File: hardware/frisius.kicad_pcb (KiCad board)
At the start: 4 copper layers, 40 x 60 mm, 133 parts, among them J1 Conn_02x20_Odd_Even_Shielded, J3 USB_C_Receptacle, J4 MEM2067, Q1 Q_NMOS_DGS, Q2 MBT2222ADW1T1, SW1 OVERRIDE, SW2 SW_Push, SW3 SW_Push, SW4 SW_Push, U1 ESP32-PICO-V3-02, U10 CP2102N-Axx-xQFN24, U12 RT5789, U13 MAX8881EUT33+T, U2 FXOS8700CQR1, U3 MS5637-02BA03, U4 L96-M33, U5 MAX77751, U6 LM75B, U7 MAX17048G

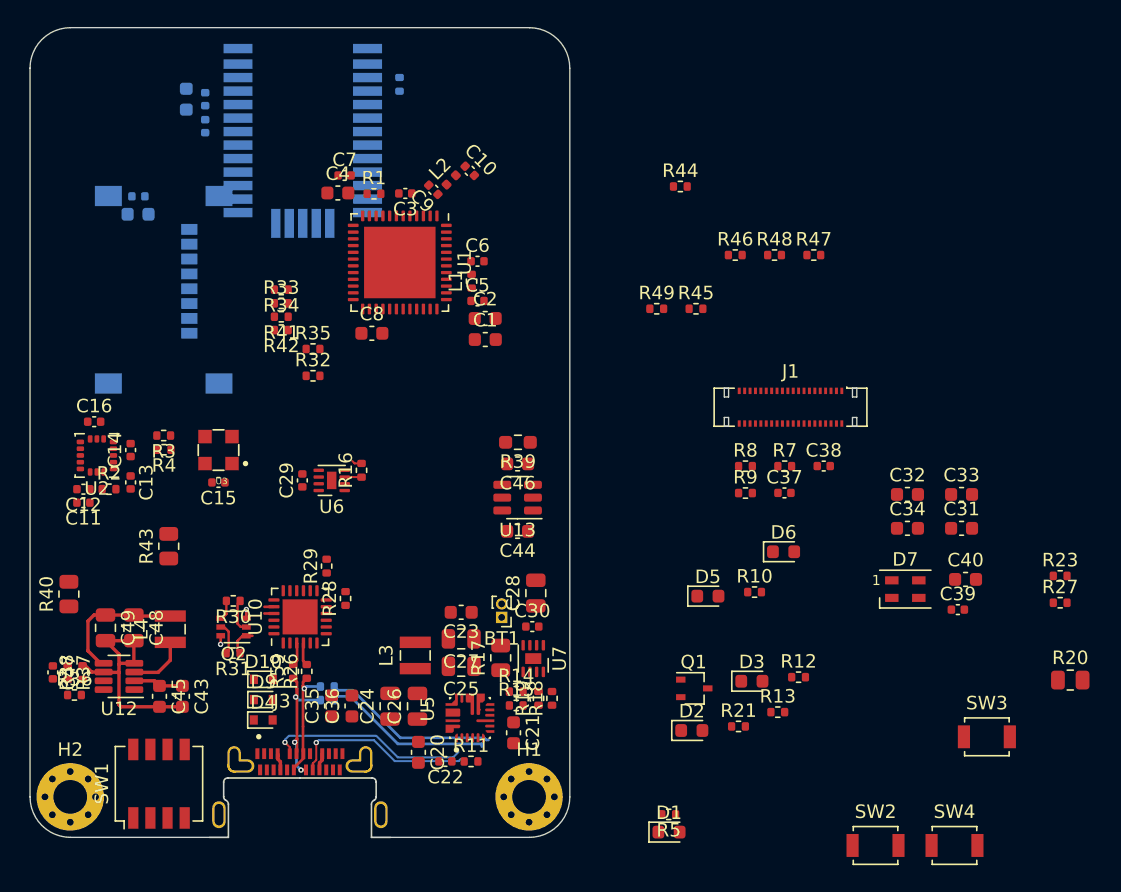
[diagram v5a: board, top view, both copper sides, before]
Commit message: schematic tidy up, component placement, shielding investigation
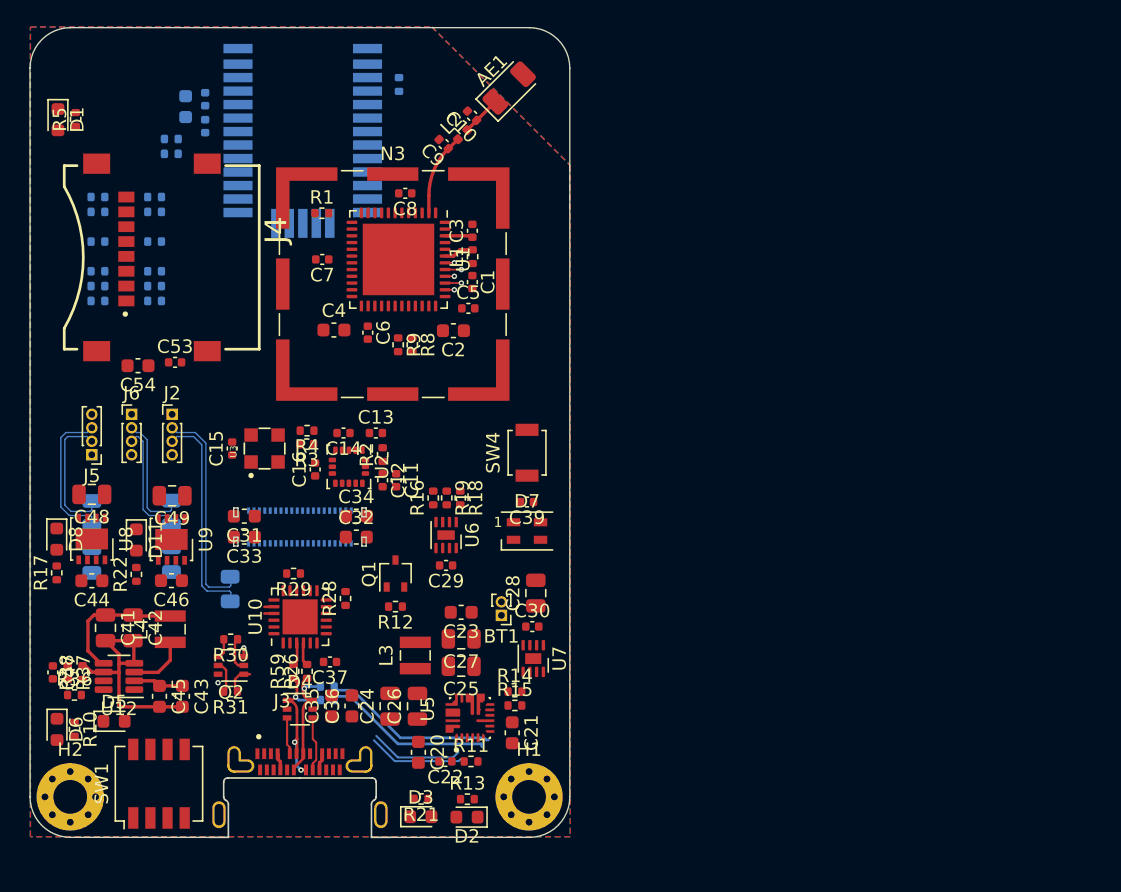
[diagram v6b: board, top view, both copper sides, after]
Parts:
- removed C38: 0.1u, Capacitor_SMD:C_0402_1005Metric
- removed C40: 1u, Capacitor_SMD:C_0603_1608Metric
- removed D10, D9: TVS, Diode_SMD:D_SOD-523
- removed R7: 0, Resistor_SMD:R_0402_1005Metric
- removed SW2, SW3: SW_Push, Button_Switch_SMD:SW_SPST_B3U-1000P
- removed U13: MAX8881EUT33+T, Package_TO_SOT_SMD:SOT-23-6
- added AE1: 2.4G, RF_Antenna:Johanson_2450AT18x100, F.Cu at (150.1, 38.4)
- added C41: 10u, Capacitor_SMD:C_0805_2012Metric, F.Cu at (120.2, 78.4)
- added C42: 10u, Capacitor_SMD:C_0805_2012Metric, F.Cu at (122.2, 78.4)
- added D11: LED_Small_Filled, LED_SMD:LED_0603_1608Metric, F.Cu at (122.5, 71.9)
- added D8: LED_Small_Filled, LED_SMD:LED_0603_1608Metric, F.Cu at (116.6, 71.8)
- added J2: Conn_01x04_Male, Connector_PinHeader_1.00mm:PinHeader_1x04_P1.00mm_Vertical, F.Cu at (125.2, 62.5)
- added J5: Conn_01x04_Male, Connector_PinHeader_1.00mm:PinHeader_1x04_P1.00mm_Vertical, F.Cu at (119.2, 65.5)
- added J6: Conn_01x04_Male, Connector_PinHeader_1.00mm:PinHeader_1x04_P1.00mm_Vertical, F.Cu at (122.2, 62.5)
- added N3: ShieldCan_ESP, RF_Shielding:Laird_Technologies_BMI-S-102_16.50x16.50mm, F.Cu at (141.5, 52.9)
- added R22: 1k, Resistor_SMD:R_0402_1005Metric, F.Cu at (122.5, 74.4)
- added R50: 0, Resistor_SMD:R_0805_2012Metric, B.Cu at (125.1, 73.3)
- added U8: NCV8187AMLExCG, Package_DFN_QFN:DFN-8-1EP_3x3mm_P0.65mm_EP1.55x2.4mm, F.Cu at (119.2, 71.8)
- added U9: NCV8187AMLExCG, Package_DFN_QFN:DFN-8-1EP_3x3mm_P0.65mm_EP1.55x2.4mm, F.Cu at (125.1, 71.8)
- C1, C8: value 1u -> 0.1u; footprint Capacitor_SMD:C_0603_1608Metric -> Capacitor_SMD:C_0402_1005Metric
- C46: value 4.7u -> 1u
- C53, C54, J4: moved to F.Cu
- D4: value TVS -> ESD5V5U5ULCE6327HTSA1; footprint Diode_SMD:D_SOD-523 -> Package_TO_SOT_SMD:SOT-363_SC-70-6
- J1, R20, R23, R27, R32, R33, R34, R35, R40, R41, R42, R43, R44, R45, R46, R47, R48, R49: moved to B.Cu
- R17: value 0 -> 1k; footprint Resistor_SMD:R_0805_2012Metric -> Resistor_SMD:R_0402_1005Metric
- R39: footprint Resistor_SMD:R_0603_1608Metric_Pad0.98x0.95mm_HandSolder -> Resistor_SMD:R_0805_2012Metric; moved to B.Cu
- moved R27 74.3 mm to (125.1, 42.1)
- moved R23 72.9 mm to (125.1, 43.2)
- moved D1 69.5 mm to (116.7, 40.7), turned to -90 degrees
- moved R5 67.7 mm to (118.0, 40.7), turned to 90 degrees
- moved R20 62.6 mm to (129.4, 75.5), turned to 90 degrees
- moved D6 55.4 mm to (116.6, 85.9), turned to -90 degrees
- moved C33 53.2 mm to (130.5, 71.7), turned to 180 degrees
- moved C31 53.2 mm to (130.5, 70.1), turned to 180 degrees
- moved R47 53.1 mm to (119.7, 49.8)
- moved R10 51.4 mm to (117.9, 85.9), turned to -90 degrees
- moved R48 50.2 mm to (119.7, 47.5)
- moved R46 47.2 mm to (119.7, 52.0)
- moved D5 45.0 mm to (120.8, 85.3)
- moved R45 44.4 mm to (119.7, 53.0)
- moved R44 44.0 mm to (119.7, 54.1)
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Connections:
- C17 pad 1: VCC_BKUP_3V3 -> VDD_NVDC
- C29 pad 1: +BATT -> VDD_NVDC
- C31 pad 2: Net-(J1-Pad1) -> Net-(C31-Pad2)
- C32 pad 1: VCC_BKUP_3V3 -> VDD_NVDC
- C32 pad 2: Net-(J1-Pad1) -> Net-(C31-Pad2)
- C33 pad 2: Net-(J1-Pad1) -> Net-(C31-Pad2)
- C34 pad 1: VCC_BKUP_3V3 -> VDD_NVDC
- C34 pad 2: Net-(J1-Pad1) -> Net-(C31-Pad2)
- C37 pad 2: VDD_USB_3V3 -> 3V3_CORE
- C44 pad 1: VDD_NVDC -> VDD_SYS_3V5
- C46 pad 1: Net-(C46-Pad1) -> VDD_SYS_3V5
- C47 pad 1: Net-(C47-Pad1) -> VDD_SYS_3V5
- C48 pad 1: Net-(C47-Pad1) -> /Power/VDD_AUX_S+
- C49 pad 1: Net-(C47-Pad1) -> /Power/VDD_CORE_S+
- C6 pad 1: /Processor/3V3_ESP_VDDA_FILT -> Net-(C6-Pad1)
- C8 pad 1: Net-(C8-Pad1) -> /Processor/3V3_ESP_VDDA_FILT
- D4 pad 1: GND -> /USB/PORT_D+
- D4 pad 2: VBUS -> GND
- D5 pad 2: /Display B2B/USR_BTN.PWR -> /Power/BOOTSTRAP
- D6 pad 2: Net-(C47-Pad1) -> Net-(D6-Pad2)
- J1 pad 1: Net-(J1-Pad1) -> Net-(C31-Pad2)
- J1 pad 11: Net-(J1-Pad1) -> Net-(C31-Pad2)
- J1 pad 12: Net-(J1-Pad1) -> Net-(C31-Pad2)
- J1 pad 13: Net-(J1-Pad1) -> unconnected-(J1-Pad13)
- J1 pad 14: Net-(J1-Pad1) -> unconnected-(J1-Pad14)
- J1 pad 17: Net-(J1-Pad1) -> Net-(C31-Pad2)
- J1 pad 2: Net-(J1-Pad1) -> Net-(C31-Pad2)
- J1 pad 22: Net-(J1-Pad1) -> Net-(C31-Pad2)
- J1 pad 28: Net-(J1-Pad1) -> Net-(C31-Pad2)
- J1 pad 29: Net-(J1-Pad1) -> Net-(C31-Pad2)
- J1 pad 3: Net-(J1-Pad1) -> Net-(C31-Pad2)
- J1 pad 33: Net-(J1-Pad1) -> Net-(C31-Pad2)
- J1 pad 34: Net-(J1-Pad1) -> Net-(C31-Pad2)
- J1 pad 35: VCC_BKUP_3V3 -> VDD_NVDC
- J1 pad 36: VCC_BKUP_3V3 -> VDD_NVDC
- J1 pad 37: VCC_BKUP_3V3 -> VDD_NVDC
- J1 pad 38: VCC_BKUP_3V3 -> VDD_NVDC
- J1 pad 39: Net-(J1-Pad1) -> Net-(C31-Pad2)
- J1 pad 4: Net-(J1-Pad1) -> Net-(C31-Pad2)
- J1 pad 40: Net-(J1-Pad1) -> Net-(C31-Pad2)
- L4 pad 2: Net-(C47-Pad1) -> VDD_SYS_3V5
- R10 pad 1: GND -> VDD_NVDC
- R10 pad 2: Net-(D6-Pad1) -> Net-(D6-Pad2)
- R17 pad 1: Net-(R17-Pad1) -> VDD_SYS_3V5
- R17 pad 2: +BATT -> Net-(D8-Pad2)
- R18 pad 1: 3V3_CORE -> VDD_AUX_3V3
- R19 pad 1: 3V3_CORE -> VDD_AUX_3V3
- R20 pad 1: Net-(R20-Pad1) -> VDD_SYS_3V5
- R20 pad 2: VDD_DISP_3V3 -> VDD_DISP_3V5
- R28 pad 2: VDD_USB_3V3 -> 3V3_CORE
- R36 pad 2: Net-(C47-Pad1) -> VDD_SYS_3V5
- R37 pad 1: Net-(C47-Pad1) -> VDD_SYS_3V5
- R39 pad 1: Net-(C46-Pad1) -> VDD_SYS_3V5
- R39 pad 2: VCC_BKUP_3V3 -> /Power/VDD_AUX_S+
- R40 pad 1: Net-(C47-Pad1) -> /Power/VDD_CORE_S+
- R43 pad 1: VDD_SYS_3V3 -> /Power/VDD_AUX_S+
- U1 pad 10: /Display B2B/USR_BTN.PWR -> /Processor/USR_BTN.PWR
- U1 pad 26: Net-(C8-Pad1) -> Net-(C6-Pad1)
- U1 pad 8: /Display B2B/USR_BTN.NAV_A -> /Processor/USR_BTN.NAV_A
- U10 pad 5: VDD_USB_3V3 -> 3V3_CORE
- U10 pad 6: VDD_USB_3V3 -> 3V3_CORE
- U10 pad 7: Net-(R7-Pad1) -> 3V3_CORE
- U12 pad 1: unconnected-(U12-Pad1) -> Net-(D6-Pad1)
- U12 pad 5: Net-(C47-Pad1) -> VDD_SYS_3V5
- U4 pad 8: VCC_BKUP_3V3 -> VDD_NVDC
- U6 pad 8: +BATT -> VDD_NVDC
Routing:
- net VDD_SYS_3V5: track 0.00 -> 26.1 mm
- net VDD_DISP_3V5: track 0.00 -> 16.1 mm
- net /Power/VDD_AUX_S+: track 0.00 -> 11.0 mm
- net Net-(C47-Pad1): track 10.1 -> 0.00 mm
- net VDD_AUX_3V3: track 0.00 -> 10.0 mm
- net 3V3_CORE: track 0.00 -> 9.19 mm
- net /Power/VDD_CORE_S+: track 0.00 -> 9.17 mm
- net Net-(C9-Pad1): track 0.00 -> 6.12 mm
- net /Processor/3V3_ESP_VDDA_FILT: track 0.00 -> 4.26 mm
- net /BMS/USB_CC.1: track 15.0 -> 11.5 mm, vias 1 -> 0
- net Net-(AE1-Pad1): track 0.00 -> 2.95 mm
- net /BMS/USB_CC.2: track 13.6 -> 11.2 mm, vias 1 -> 0
- net /BMS/THERM_SHDN: track 1.25 -> 0.00 mm
- net /Processor/DEBUG_UART.TXD: track 0.00 -> 1.21 mm, vias 0 -> 1
- net /Display B2B/DISPLAY.DC: track 0.00 -> 1.21 mm, vias 0 -> 1
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- added copper zone on B.Cu, net GND
- added copper zone on F.Cu, net GND

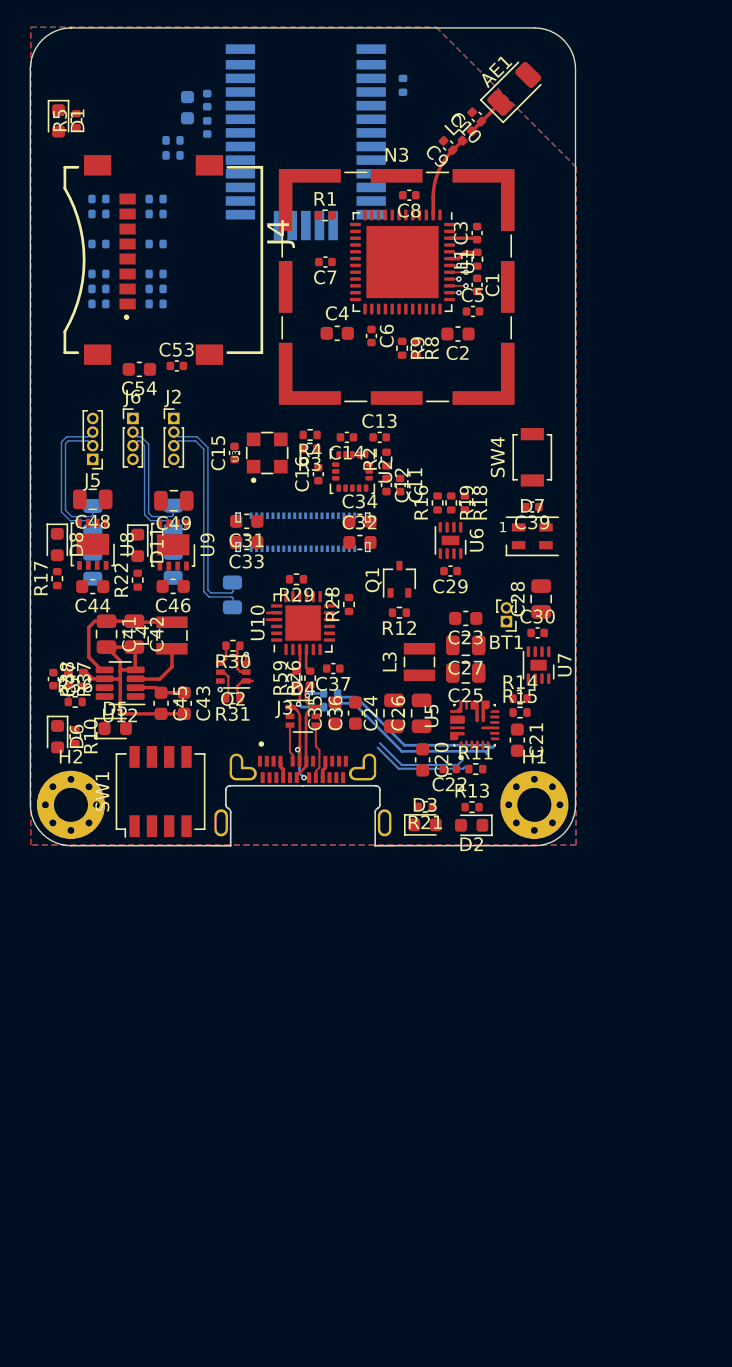
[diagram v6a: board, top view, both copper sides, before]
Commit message: minor sch tweaks, more layout, added power emc shield
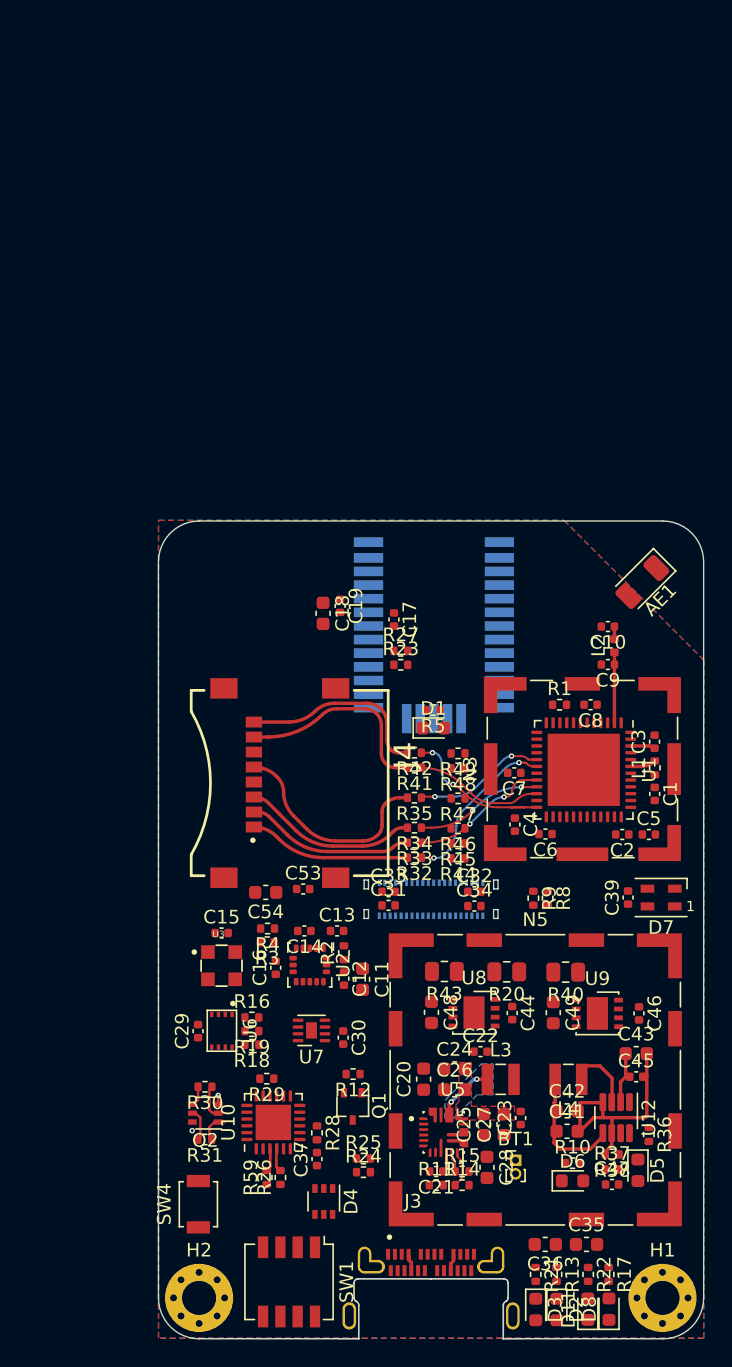
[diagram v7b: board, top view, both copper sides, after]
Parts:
- removed J2, J5, J6: Conn_01x04_Male, Connector_PinHeader_1.00mm:PinHeader_1x04_P1.00mm_Vertical
- removed R39, R50: 0, Resistor_SMD:R_0805_2012Metric
- removed R6: 0, Resistor_SMD:R_0402_1005Metric
- added N5: SheildCan_Power, RF_Shielding:Wuerth_36103205_20x20mm, F.Cu at (151.7, 111.1)
- C11: footprint Capacitor_SMD:C_0402_1005Metric -> Capacitor_SMD:C_0603_1608Metric
- C17, C18, C19, R20, R23, R24, R25, R27, R32, R33, R34, R35, R40, R41, R42, R43, R44, R45, R46, R47, R48, R49: moved to F.Cu
- C2, C31, C32, C33, C34, C4, C44, C45, C46: footprint Capacitor_SMD:C_0603_1608Metric -> Capacitor_SMD:C_0402_1005Metric
- C21, C23: value 4.7u -> 1u; footprint Capacitor_SMD:C_0603_1608Metric -> Capacitor_SMD:C_0402_1005Metric
- C24, C25, C26, C27, C28, C41, C42, C48, C49: footprint Capacitor_SMD:C_0805_2012Metric -> Capacitor_SMD:C_0603_1608Metric
- N3: footprint RF_Shielding:Laird_Technologies_BMI-S-102_16.50x16.50mm -> RF_Shielding:Laird_Technologies_BMI-S-101_13.66x12.70mm
- U6: footprint Package_DFN_QFN:DFN-8-1EP_2x2mm_P0.5mm_EP0.7x1.3mm -> bt_Package_SON:XSON-8U
- moved D8 69.2 mm to (157.1, 127.9), turned to 90 degrees
- moved R17 65.1 mm to (157.1, 125.3), turned to -90 degrees
- moved D11 65.0 mm to (155.5, 127.9), turned to 90 degrees
- moved R22 60.7 mm to (155.6, 125.3), turned to -90 degrees
- moved SW4 60.0 mm to (127.0, 120.2)
- moved C47 55.3 mm to (157.3, 118.8), turned to 0 degrees
- moved R37 53.7 mm to (157.3, 117.7), turned to 0 degrees
- moved R36 52.7 mm to (160.0, 115.1), turned to -90 degrees
- moved D1 52.3 mm to (144.2, 85.3), turned to 0 degrees
- moved R38 52.2 mm to (157.3, 116.5), turned to 180 degrees
- moved R5 50.6 mm to (144.2, 84.0), turned to 180 degrees
- moved D5 50.2 mm to (159.2, 117.7), turned to -90 degrees
- moved D6 49.9 mm to (154.4, 118.5), turned to 0 degrees
- moved C41 49.7 mm to (154.0, 114.8), turned to 0 degrees
- moved R45 48.5 mm to (146.0, 93.7), turned to 180 degrees
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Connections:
- net /Power/VDD_AUX_S+ renamed Net-(C48-Pad1)
- net /Power/VDD_CORE_S+ renamed Net-(C49-Pad1)
- AE1 pad 1: Net-(AE1-Pad1) -> unconnected-(AE1-Pad1)
- AE1 pad 2: GND -> Net-(AE1-Pad2)
- C1 pad 1: 3V3_CORE -> VDD_CORE_3V3
- C10 pad 1: Net-(AE1-Pad1) -> Net-(AE1-Pad2)
- C15 pad 2: Net-(C15-Pad2) -> GND
- C2 pad 1: 3V3_CORE -> VDD_CORE_3V3
- C31 pad 2: Net-(C31-Pad2) -> GND
- C32 pad 2: Net-(C31-Pad2) -> GND
- C33 pad 2: Net-(C31-Pad2) -> GND
- C34 pad 2: Net-(C31-Pad2) -> GND
- C37 pad 2: 3V3_CORE -> VDD_CORE_3V3
- C4 pad 1: 3V3_CORE -> VDD_CORE_3V3
- C5 pad 1: 3V3_CORE -> VDD_CORE_3V3
- C7 pad 1: 3V3_CORE -> VDD_CORE_3V3
- D2 pad 2: VDD_USB_3V3 -> VDD_CORE_3V3
- D3 pad 2: VDD_USB_3V3 -> VDD_CORE_3V3
- J1 pad 1: Net-(C31-Pad2) -> GND
- J1 pad 11: Net-(C31-Pad2) -> GND
- J1 pad 12: Net-(C31-Pad2) -> GND
- J1 pad 17: Net-(C31-Pad2) -> GND
- J1 pad 2: Net-(C31-Pad2) -> GND
- J1 pad 22: Net-(C31-Pad2) -> GND
- J1 pad 28: Net-(C31-Pad2) -> GND
- J1 pad 29: Net-(C31-Pad2) -> GND
- J1 pad 3: Net-(C31-Pad2) -> GND
- J1 pad 33: Net-(C31-Pad2) -> GND
- J1 pad 34: Net-(C31-Pad2) -> GND
- J1 pad 39: Net-(C31-Pad2) -> GND
- J1 pad 4: Net-(C31-Pad2) -> GND
- J1 pad 40: Net-(C31-Pad2) -> GND
- L1 pad 1: 3V3_CORE -> VDD_CORE_3V3
- L2 pad 2: Net-(AE1-Pad1) -> Net-(AE1-Pad2)
- R1 pad 1: 3V3_CORE -> VDD_CORE_3V3
- R11 pad 2: VDD_USB_3V3 -> VDD_CORE_3V3
- R12 pad 2: VDD_USB_3V3 -> VDD_CORE_3V3
- R28 pad 2: 3V3_CORE -> VDD_CORE_3V3
- R40 pad 2: 3V3_CORE -> VDD_CORE_3V3
- R44 pad 2: Net-(J4-Pad1) -> /Processor/SDMMC.D2
- R45 pad 2: Net-(J4-Pad2) -> /Processor/SDMMC.D3
- R46 pad 2: Net-(J4-Pad3) -> /Processor/SDMMC.CMD
- R47 pad 2: Net-(J4-Pad5) -> /Processor/SDMMC.CLK
- R48 pad 2: Net-(J4-Pad7) -> /Processor/SDMMC.D0
- R49 pad 2: Net-(J4-Pad8) -> /Processor/SDMMC.D1
- U1 pad 19: 3V3_CORE -> VDD_CORE_3V3
- U1 pad 37: 3V3_CORE -> VDD_CORE_3V3
- U10 pad 5: 3V3_CORE -> VDD_CORE_3V3
- U10 pad 6: 3V3_CORE -> VDD_CORE_3V3
- U10 pad 7: 3V3_CORE -> VDD_CORE_3V3
- U3 pad 4: Net-(C15-Pad2) -> GND
- U4 pad 16: Net-(R6-Pad2) -> /GPS/GPS_RF
- U5 pad 13_14: Net-(R17-Pad1) -> +BATT
- U5 pad 2: /Processor/USB_PRESENT -> Net-(Q1-Pad2)
- U5 pad 3: Net-(R13-Pad2) -> Net-(R21-Pad1)
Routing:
- net VDD_DISP_3V5: track 16.1 -> 0.00 mm
- net Net-(J4-Pad5): track 0.00 -> 16.1 mm
- net VDD_SYS_3V5: track 26.1 -> 10.1 mm
- net Net-(J4-Pad7): track 0.00 -> 15.1 mm
- net Net-(J4-Pad8): track 0.00 -> 14.1 mm
- net /BMS/USB_CHG.D-: track 13.1 -> 0.00 mm
- net Net-(J4-Pad3): track 0.00 -> 12.8 mm
- net /BMS/USB_CHG.D+: track 12.7 -> 0.00 mm
- net Net-(J4-Pad2): track 0.00 -> 12.3 mm
- net /Processor/SDMMC.D2: track 0.00 -> 12.2 mm, vias 0 -> 2
- net Net-(J4-Pad1): track 0.00 -> 11.8 mm
- net /Processor/SDMMC.D1: track 0.00 -> 11.6 mm, vias 0 -> 2
- net /BMS/USB_CC.1: track 11.5 -> 0.00 mm
- net /USB/PORT_D+: track 11.3 -> 0.00 mm, vias 3 -> 0
- net /BMS/USB_CC.2: track 11.2 -> 0.00 mm
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- added copper zone on B.Cu, net Net-(C22-Pad2)
